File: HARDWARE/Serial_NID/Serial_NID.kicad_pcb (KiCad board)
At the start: 2 copper layers, 40 x 20.3 mm, 14 parts, among them J1 CONN_01X04, J2 CONN_01X07, J3 USB_OTG, U1 TPS2550, U2 STM32L011Gx, U3 FT230XQ

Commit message: updated pcb
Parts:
- added C6: C, ZF_footprints:ZF_SMD_NonPol_0402_cap, F.Cu at (125.2, 104.1)
- added C7: C, ZF_footprints:ZF_SMD_NonPol_0402_cap, F.Cu at (125.2, 103.4)
- added C8: C, ZF_footprints:ZF_SMD_NonPol_0402_cap, F.Cu at (148.6, 105.2)
- added D1: LED, ZF_footprints:ZF_SMD_NonPol_0402, F.Cu at (128.1, 94.4)
- added R4: R, ZF_footprints:ZF_SMD_NonPol_0402, F.Cu at (125.2, 104.9)
- added R5: R, ZF_footprints:ZF_SMD_NonPol_0402, F.Cu at (125.2, 102.6)
- added R6: R, ZF_footprints:ZF_SMD_NonPol_0402, F.Cu at (136.3, 106.8)
- added R7: R, ZF_footprints:ZF_SMD_NonPol_0402, F.Cu at (130.4, 94.4)
- added SW1: SW_PUSH, ZF_footprints:ZF_SW_Momentary_SideMtg, F.Cu at (141.6, 110.5)
- C1, C2, C3, C4, C5: footprint Capacitors_SMD:C_0603_HandSoldering -> ZF_footprints:ZF_SMD_NonPol_0402_cap
- J3: footprint Connectors:USB_Micro-B -> ZF_footprints:JW_USBMICROB_SMT
- R1, R2, R3: footprint Resistors_SMD:R_0603 -> ZF_footprints:ZF_SMD_NonPol_0402
- U2: footprint Housings_DFN_QFN:UQFN-28-1EP_4x4mm_Pitch0.4mm -> ZF_footprints:ZF_IC_UFQFPN28-050
- moved C5 43.3 mm to (148.6, 108.2), turned to 0 degrees
- moved C4 43.2 mm to (148.6, 109.2), turned to 0 degrees
- moved J1 37.1 mm to (160.7, 103.6)
- moved R3 36.4 mm to (153.8, 105.2), turned to 0 degrees
- moved C2 36.1 mm to (144.1, 98.2), turned to 0 degrees
- moved U1 34.9 mm to (149.9, 101.3), turned to 270 degrees
- moved U3 31.0 mm to (129.7, 103.8)
- moved J2 30.9 mm to (141.0, 93.0)
- moved C1 30.9 mm to (129.7, 108.8), turned to 0 degrees
- moved J3 30.0 mm to (119.4, 104.1)
- moved U2 27.9 mm to (139.2, 101.5), turned to 180 degrees
- moved R1 27.3 mm to (134.2, 97.2)
- moved C3 26.3 mm to (125.2, 108.5)
- moved R2 18.7 mm to (129.7, 107.9), turned to 180 degrees
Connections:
- J3 pad 2: Net-(J3-Pad2) -> Net-(C7-Pad1)
- J3 pad 3: Net-(J3-Pad3) -> Net-(C6-Pad2)
- U1 pad 3: +5V -> EN
- U2 pad 10: Net-(U2-Pad10) -> CBUS2
- U2 pad 11: Net-(U2-Pad11) -> CBUS3
- U2 pad 13: Net-(U2-Pad13) -> FAULT
- U2 pad 14: Net-(U2-Pad14) -> EN
- U2 pad 6: Net-(U2-Pad6) -> LED1
- U2 pad 8: Net-(U2-Pad8) -> CBUS0
- U2 pad 9: Net-(U2-Pad9) -> CBUS1
- U3 pad 1: Net-(U3-Pad1) -> +3V3
- U3 pad 11: Net-(U3-Pad11) -> CBUS1
- U3 pad 12: Net-(U3-Pad12) -> CBUS0
- U3 pad 14: Net-(U3-Pad14) -> CBUS3
- U3 pad 5: Net-(U3-Pad5) -> CBUS2
- U3 pad 6: Net-(J3-Pad3) -> Net-(R5-Pad1)
- U3 pad 7: Net-(J3-Pad2) -> Net-(R4-Pad1)
- U3 pad 9: Net-(U3-Pad9) -> +3V3
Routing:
- net EN: track 0.00 -> 23.2 mm
- net FAULT: track 4.23 -> 27.4 mm, vias 0 -> 4
- net +5V: track 33.3 -> 52.0 mm, vias 4 -> 6
- net GND: track 43.7 -> 27.8 mm, vias 2 -> 11
- net A1IN: track 11.3 -> 26.6 mm, vias 0 -> 2
- net SWDIO: track 9.57 -> 22.6 mm, vias 0 -> 2
- net CBUS2: track 0.00 -> 12.9 mm, vias 0 -> 2
- net CBUS1: track 0.00 -> 11.3 mm
- net +3V3: track 25.7 -> 35.9 mm, vias 0 -> 5
- net LED1: track 0.00 -> 9.76 mm
- net CBUS0: track 0.00 -> 9.61 mm
- net SWITCH: track 0.00 -> 8.66 mm, vias 0 -> 2
- net SWCLK: track 9.74 -> 17.6 mm, vias 0 -> 2
- net +5VD: track 29.2 -> 36.6 mm, vias 3 -> 4
- net A1EX: track 13.4 -> 20.7 mm
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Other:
- board size 40 x 20.3 mm -> 48.7 x 24 mm
- net class Default: trace_width 0.15 -> 0.2
- net class POWEr added: clearance 0.1, trace_width 0.5, via_dia 0.6, via_drill 0.4
- rule pad_to_mask_clearance: 0.2 -> 0
- rule trace_min: 0.1 -> 0.2
- board text added: "ID"
- board text added: "Supplying Power 450 mA limited"
- board text added: "USB Power + Network Interface"

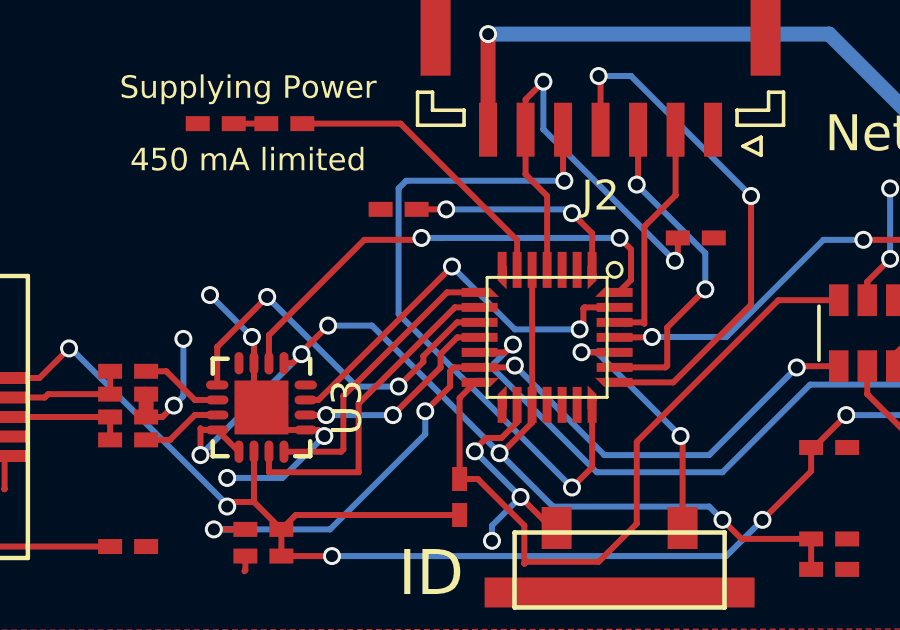
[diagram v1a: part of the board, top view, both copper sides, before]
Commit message: updated TX RX
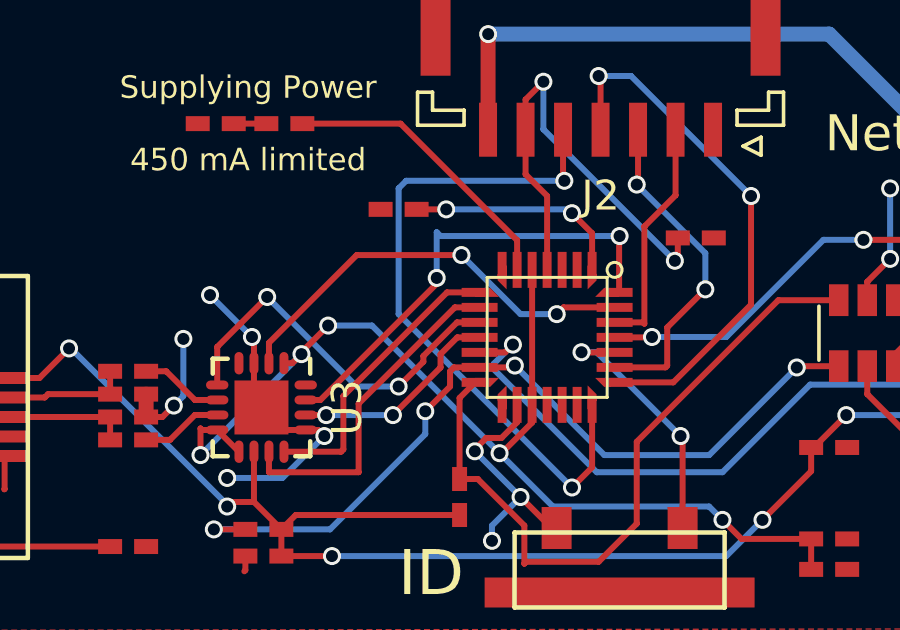
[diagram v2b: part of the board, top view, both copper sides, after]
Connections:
- U2 pad 27: USART2_RX -> USART2_TX
- U2 pad 28: USART2_TX -> USART2_RX
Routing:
- net USART2_RX: track 13.6 -> 15.8 mm
- net USART2_TX: track 16.1 -> 14.3 mm
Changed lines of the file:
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@@
     (links 75)
     (no_connects 3)
-    (area 0 0 0 0)
+    (area 115.773999 87.452999 164.550001 111.550001)
     (thickness 1.6)
     (drawings 9)
-    (tracks 307)
+    (tracks 306)
     (zones 0)
     (modules 23)
@@
       (net 12 MOSI))
     (pad 27 smd rect (at -2.246733 0.986815 90) (size 0.3 1.2) (layers F.Cu F.Paste F.Mask)
+      (net 37 USART2_TX))
+    (pad 28 smd rect (at -2.396733 1.486815 90) (size 0.3 0.9) (layers F.Cu F.Paste F.Mask)
       (net 36 USART2_RX))
-    (pad 28 smd rect (at -2.396733 1.486815 90) (size 0.3 0.9) (layers F.Cu F.Paste F.Mask)
-      (net 37 USART2_TX))
     (pad 1 smd trapezoid (at -1.496733 1.986815) (size 0.3 0.5) (rect_delta 0.3 0 ) (layers F.Cu F.Paste F.Mask)
       (net 17 "Net-(R1-Pad1)"))
     (pad 28 smd trapezoid (at -1.996733 1.486815 90) (size 0.3 0.5) (rect_delta 0.3 0 ) (layers F.Cu F.Paste F.Mask)
-      (net 37 USART2_TX))
+      (net 36 USART2_RX))
     (pad 14 smd trapezoid (at 2.003267 -1.513185 270) (size 0.3 0.5) (rect_delta 0.3 0 ) (layers F.Cu F.Paste F.Mask)
       (net 22 EN))
@@
   (via (at 131.826 104.0765) (size 0.6) (drill 0.4) (layers F.Cu B.Cu) (net 31))
   (segment (start 131.822 104.0725) (end 131.826 104.0765) (width 0.2) (layer F.Cu) (net 31))
-  (segment (start 131.142 103.5725) (end 131.568 103.5725) (width 0.2) (layer F.Cu) (net 36))
-  (segment (start 140.432815 100.486185) (end 141.438733 100.486185) (width 0.2) (layer F.Cu) (net 36))
-  (segment (start 140.3985 100.5205) (end 140.432815 100.486185) (width 0.2) (layer F.Cu) (net 36))
-  (segment (start 140.3985 101.092) (end 140.3985 100.5205) (width 0.2) (layer F.Cu) (net 36))
-  (segment (start 140.2715 101.219) (end 140.3985 101.092) (width 0.2) (layer F.Cu) (net 36))
-  (via (at 140.2715 101.219) (size 0.6) (drill 0.4) (layers F.Cu B.Cu) (net 36))
-  (segment (start 138.1125 101.219) (end 140.2715 101.219) (width 0.2) (layer B.Cu) (net 36))
-  (segment (start 136.017 99.1235) (end 138.1125 101.219) (width 0.2) (layer B.Cu) (net 36))
-  (via (at 136.017 99.1235) (size 0.6) (drill 0.4) (layers F.Cu B.Cu) (net 36))
-  (segment (start 131.568 103.5725) (end 136.017 99.1235) (width 0.2) (layer F.Cu) (net 36))
-  (segment (start 141.588733 99.986185) (end 141.588733 99.965267) (width 0.2) (layer F.Cu) (net 37))
-  (segment (start 141.588733 99.965267) (end 141.986 99.568) (width 0.2) (layer F.Cu) (net 37))
-  (segment (start 141.986 99.568) (end 141.986 98.552) (width 0.2) (layer F.Cu) (net 37))
-  (segment (start 141.986 98.552) (end 141.605 98.171) (width 0.2) (layer F.Cu) (net 37))
-  (via (at 141.605 98.171) (size 0.6) (drill 0.4) (layers F.Cu B.Cu) (net 37))
-  (segment (start 141.605 98.171) (end 135.636 98.171) (width 0.2) (layer B.Cu) (net 37))
-  (segment (start 135.636 98.171) (end 135.001 98.171) (width 0.2) (layer B.Cu) (net 37))
-  (via (at 135.001 98.171) (size 0.6) (drill 0.4) (layers F.Cu B.Cu) (net 37))
-  (segment (start 135.001 98.171) (end 134.9375 98.2345) (width 0.2) (layer F.Cu) (net 37))
-  (segment (start 134.9375 98.2345) (end 133.096 98.2345) (width 0.2) (layer F.Cu) (net 37))
-  (segment (start 133.096 98.2345) (end 129.917 101.4135) (width 0.2) (layer F.Cu) (net 37))
-  (segment (start 129.917 101.4135) (end 129.917 102.3475) (width 0.2) (layer F.Cu) (net 37))
+  (segment (start 131.142 103.5725) (end 131.6315 103.5725) (width 0.2) (layer F.Cu) (net 36) (status 400000))
+  (segment (start 141.588733 98.123767) (end 141.588733 99.986185) (width 0.2) (layer F.Cu) (net 36) (status 800000))
+  (segment (start 141.605 98.1075) (end 141.588733 98.123767) (width 0.2) (layer F.Cu) (net 36))
+  (via (at 141.605 98.1075) (size 0.6) (drill 0.4) (layers F.Cu B.Cu) (net 36))
+  (segment (start 135.636 98.1075) (end 141.605 98.1075) (width 0.2) (layer B.Cu) (net 36))
+  (segment (start 135.509 97.9805) (end 135.636 98.1075) (width 0.2) (layer B.Cu) (net 36))
+  (segment (start 135.509 99.5045) (end 135.509 97.9805) (width 0.2) (layer B.Cu) (net 36))
+  (via (at 135.509 99.5045) (size 0.6) (drill 0.4) (layers F.Cu B.Cu) (net 36))
+  (segment (start 135.5725 99.568) (end 135.509 99.5045) (width 0.2) (layer F.Cu) (net 36))
+  (segment (start 135.5725 99.6315) (end 135.5725 99.568) (width 0.2) (layer F.Cu) (net 36))
+  (segment (start 131.6315 103.5725) (end 135.5725 99.6315) (width 0.2) (layer F.Cu) (net 36))
+  (segment (start 141.588733 99.986185) (end 141.588733 99.965267) (width 0.2) (layer F.Cu) (net 36))
+  (segment (start 129.917 102.3475) (end 129.917 101.6675) (width 0.2) (layer F.Cu) (net 37) (status 400000))
+  (segment (start 139.734315 100.486185) (end 141.438733 100.486185) (width 0.2) (layer F.Cu) (net 37) (status 800000))
+  (segment (start 139.5095 100.711) (end 139.734315 100.486185) (width 0.2) (layer F.Cu) (net 37))
+  (via (at 139.5095 100.711) (size 0.6) (drill 0.4) (layers F.Cu B.Cu) (net 37))
+  (segment (start 138.303 100.711) (end 139.5095 100.711) (width 0.2) (layer B.Cu) (net 37))
+  (segment (start 136.3345 98.7425) (end 138.303 100.711) (width 0.2) (layer B.Cu) (net 37))
+  (via (at 136.3345 98.7425) (size 0.6) (drill 0.4) (layers F.Cu B.Cu) (net 37))
+  (segment (start 132.842 98.7425) (end 136.3345 98.7425) (width 0.2) (layer F.Cu) (net 37))
+  (segment (start 129.917 101.6675) (end 132.842 98.7425) (width 0.2) (layer F.Cu) (net 37))
   (zone (net 1) (net_name GND) (layer F.Cu) (hatch edge 0.508)
     (connect_pads (clearance 0.508))

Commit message: fixed pcb
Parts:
- added C10: C, ZF_footprints:ZF_SMD_NonPol_0402_cap, F.Cu at (129.7, 109.7)
- added C9: C, ZF_footprints:ZF_SMD_NonPol_0402_cap, F.Cu at (129.7, 110.7)
- J1: footprint Connectors_JST:JST_GH_SM04B-GHS-TB_04x1.25mm_Angled -> ZF_footprints:ZF_CONN_JST_GH
- J2: footprint Connectors_JST:JST_GH_SM07B-GHS-TB_07x1.25mm_Angled -> ZF_footprints:ZF_CONN_JST_GH_7POS
- U3: footprint Housings_DFN_QFN:QFN-16-1EP_3x3mm_Pitch0.5mm -> Housings_DFN_QFN:QFN-16-1EP_4x4mm_Pitch0.65mm
- moved J2 2.39 mm to (141.4, 90.6), turned to 90 degrees
- moved J1 1.98 mm to (162.2, 102.4), turned to 0 degrees
- moved U3 0.63 mm to (130.3, 103.8)
- moved SW1 0.51 mm to (141.6, 111.0)
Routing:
- net CBUS0: track 9.61 -> 25.3 mm, vias 0 -> 2
- net CBUS1: track 11.3 -> 22.6 mm, vias 0 -> 2
- net GND: track 27.8 -> 38.8 mm, vias 11 -> 10
- net +3V3: track 35.9 -> 46.7 mm, vias 5 -> 6
- net +5V: track 52.0 -> 54.0 mm
- net NSS: track 11.1 -> 12.9 mm
- net MOSI: track 7.90 -> 9.69 mm
- net SWDIO: track 22.6 -> 24.3 mm
- net A1IN: track 26.6 -> 28.0 mm
- net SWCLK: track 17.6 -> 16.4 mm
- net CBUS3: track 7.13 -> 6.19 mm, vias 2 -> 0
- net USART2_TX: track 14.3 -> 13.5 mm
- net SWITCH: track 8.66 -> 9.26 mm
- net EN: track 23.2 -> 23.8 mm
- added copper zone on B.Cu, net GND
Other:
- board size 48.7 x 24 mm -> 47.5 x 23 mm
- net class Default: clearance 0.1 -> 0.2
- net class POWEr: clearance 0.1 -> 0.2
- rule trace_clearance: 0.1 -> 0.2

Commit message: fixed pcb
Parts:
- added G***: LOGO, ZF_footprints:ZF_LOGO_OSHW, F.Cu at (121.5, 95.1)
- C10: value C -> 4.7uF; footprint ZF_footprints:ZF_SMD_NonPol_0402_cap -> Resistors_SMD:R_0603_HandSoldering
- J3: footprint ZF_footprints:JW_USBMICROB_SMT -> ZF_footprints:ZF_CONN_USB-MICRO-B-SMD-holes
- moved C10 4.93 mm to (134.6, 110.4)
- moved C9 1.02 mm to (129.7, 109.7)
- moved J3 0.83 mm to (118.6, 104.1)
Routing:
- net GND: track 38.8 -> 34.4 mm, vias 10 -> 8
- net A1IN: track 28.0 -> 29.9 mm
- net Net-(C3-Pad1): track 13.8 -> 15.4 mm
- net +5V: track 54.0 -> 55.4 mm
- net +3V3: track 46.7 -> 47.8 mm

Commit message: fixd pcb
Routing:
- net +5V: track 55.4 -> 56.2 mm
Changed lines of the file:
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@@
   (general
     (links 83)
-    (no_connects 1)
-    (area 116.949999 88.449999 164.550001 111.550001)
+    (no_connects 0)
+    (area 111.8295 85.581166 167.212334 114.300001)
     (thickness 1.6)
     (drawings 7)
-    (tracks 371)
+    (tracks 366)
     (zones 0)
     (modules 26)
@@
     (46 B.CrtYd user)
     (47 F.CrtYd user)
-    (48 B.Fab user)
-    (49 F.Fab user)
+    (48 B.Fab user hide)
+    (49 F.Fab user hide)
   )
   (setup
@@
     (effects (font (size 1.33 1.33) (thickness 0.19) italic))
   )
-  (segment (start 126.4285 102.9335) (end 126.365 102.9335) (width 0.2) (layer B.Cu) (net 0))
-  (segment (start 126.365 102.997) (end 126.365 102.9335) (width 0.2) (layer B.Cu) (net 0))
   (segment (start 134.239 108.0135) (end 131.8895 110.363) (width 0.2) (layer F.Cu) (net 1))
   (via (at 136.906 105.41) (size 0.6) (drill 0.4) (layers F.Cu B.Cu) (net 1))
   (via (at 131.8895 110.363) (size 0.6) (drill 0.4) (layers F.Cu B.Cu) (net 1))
-  (segment (start 131.8895 110.363) (end 131.6355 110.617) (width 0.2) (layer B.Cu) (net 1))
   (segment (start 135.0645 106.3625) (end 135.0645 107.188) (width 0.2) (layer B.Cu) (net 1))
   (segment (start 136.144 105.283) (end 135.0645 106.3625) (width 0.2) (layer B.Cu) (net 1))
@@
   (segment (start 149.86 99.6315) (end 150.622 98.8695) (width 0.2) (layer F.Cu) (net 1))
   (segment (start 125.822 104.14) (end 125.822 103.378) (width 0.5) (layer F.Cu) (net 1))
+  (segment (start 130.3305 109.6645) (end 130.3305 108.7755) (width 0.2) (layer F.Cu) (net 2) (status C00000))
   (segment (start 135.72 110.363) (end 135.72 108.4785) (width 0.2) (layer F.Cu) (net 2))
   (segment (start 135.72 108.4785) (end 134.6485 107.407) (width 0.2) (layer F.Cu) (net 2))
@@
   (segment (start 158.272 100.487) (end 159.779 100.487) (width 0.2) (layer F.Cu) (net 11))
   (segment (start 156.0195 98.2345) (end 156.083 98.298) (width 0.2) (layer F.Cu) (net 11))
+  (segment (start 143.47 96.7505) (end 143.8275 96.393) (width 0.2) (layer F.Cu) (net 12))
+  (segment (start 142.218815 100.986185) (end 142.4305 100.7745) (width 0.2) (layer F.Cu) (net 12))
+  (segment (start 142.4305 100.7745) (end 142.4305 97.79) (width 0.2) (layer F.Cu) (net 12))
+  (segment (start 143.47 96.7505) (end 142.4305 97.79) (width 0.2) (layer F.Cu) (net 12))
   (segment (start 141.438733 100.986185) (end 142.218815 100.986185) (width 0.2) (layer F.Cu) (net 12))
-  (segment (start 143.47 96.7505) (end 142.4305 97.79) (width 0.2) (layer F.Cu) (net 12))
-  (segment (start 143.47 96.7505) (end 143.47 94.615) (width 0.2) (layer F.Cu) (net 12))
-  (segment (start 142.4305 100.7745) (end 142.4305 97.79) (width 0.2) (layer F.Cu) (net 12))
-  (segment (start 142.218815 100.986185) (end 142.4305 100.7745) (width 0.2) (layer F.Cu) (net 12))
-  (segment (start 143.47 94.615) (end 143.47 93.459) (width 0.2) (layer F.Cu) (net 12))
-  (segment (start 143.47 93.459) (end 143.9145 93.0145) (width 0.2) (layer F.Cu) (net 12))
-  (segment (start 143.47 94.564) (end 143.47 94.615) (width 0.2) (layer F.Cu) (net 12))
-  (segment (start 142.22 94.615) (end 142.22 93.459) (width 0.2) (layer F.Cu) (net 13))
-  (segment (start 142.22 93.459) (end 142.6645 93.0145) (width 0.2) (layer F.Cu) (net 13))
-  (segment (start 142.22 94.564) (end 142.22 94.615) (width 0.2) (layer F.Cu) (net 13))
-  (segment (start 142.22 94.615) (end 142.22 96.3495) (width 0.2) (layer F.Cu) (net 13))
-  (segment (start 143.131815 102.486185) (end 141.438733 102.486185) (width 0.2) (layer F.Cu) (net 13))
+  (segment (start 143.8275 96.393) (end 143.8275 93.1015) (width 0.2) (layer F.Cu) (net 12) (status 800000))
+  (segment (start 143.8275 93.1015) (end 143.9145 93.0145) (width 0.2) (layer F.Cu) (net 12) (status C00000))
+  (segment (start 144.4625 98.679) (end 144.4625 98.2345) (width 0.2) (layer B.Cu) (net 13))
+  (segment (start 144.4625 98.679) (end 144.4625 99.8855) (width 0.2) (layer B.Cu) (net 13))
+  (via (at 144.4625 99.8855) (size 0.6) (drill 0.4) (layers F.Cu B.Cu) (net 13))
+  (segment (start 144.4625 99.8855) (end 143.7005 100.6475) (width 0.2) (layer F.Cu) (net 13))
+  (segment (start 143.7005 100.6475) (end 143.7005 101.9175) (width 0.2) (layer F.Cu) (net 13))
   (segment (start 143.7005 101.9175) (end 143.131815 102.486185) (width 0.2) (layer F.Cu) (net 13))
-  (segment (start 143.7005 100.6475) (end 143.7005 101.9175) (width 0.2) (layer F.Cu) (net 13))
-  (segment (start 144.4625 99.8855) (end 143.7005 100.6475) (width 0.2) (layer F.Cu) (net 13))
-  (via (at 144.4625 99.8855) (size 0.6) (drill 0.4) (layers F.Cu B.Cu) (net 13))
-  (segment (start 144.4625 98.679) (end 144.4625 99.8855) (width 0.2) (layer B.Cu) (net 13))
-  (segment (start 142.1765 96.393) (end 144.4625 98.679) (width 0.2) (layer B.Cu) (net 13))
-  (via (at 142.1765 96.393) (size 0.6) (drill 0.4) (layers F.Cu B.Cu) (net 13))
-  (segment (start 142.22 96.3495) (end 142.1765 96.393) (width 0.2) (layer F.Cu) (net 13))
+  (segment (start 141.438733 102.486185) (end 143.131815 102.486185) (width 0.2) (layer F.Cu) (net 13))
+  (segment (start 142.6645 96.3495) (end 142.6645 93.0145) (width 0.2) (layer F.Cu) (net 13) (status 800000))
+  (segment (start 142.621 96.393) (end 142.6645 96.3495) (width 0.2) (layer F.Cu) (net 13))
+  (via (at 142.621 96.393) (size 0.6) (drill 0.4) (layers F.Cu B.Cu) (net 13))
+  (segment (start 144.4625 98.2345) (end 142.621 96.393) (width 0.2) (layer B.Cu) (net 13))
   (segment (start 145.9865 96.774) (end 145.923 96.774) (width 0.2) (layer B.Cu) (net 14))
   (segment (start 143.393815 102.986185) (end 145.9865 100.3935) (width 0.2) (layer F.Cu) (net 14))
@@
   (segment (start 144.145 94.996) (end 141.4145 94.996) (width 0.2) (layer B.Cu) (net 14))
   (segment (start 145.923 96.774) (end 144.145 94.996) (width 0.2) (layer B.Cu) (net 14))
-  (segment (start 139.72 94.564) (end 139.72 93.459) (width 0.2) (layer F.Cu) (net 15))
+  (segment (start 139.7635 96.266) (end 140.1445 95.885) (width 0.2) (layer F.Cu) (net 15))
+  (segment (start 140.1445 95.885) (end 140.1445 93.0345) (width 0.2) (layer F.Cu) (net 15) (status 800000))
+  (segment (start 140.1445 93.0345) (end 140.1645 93.0145) (width 0.2) (layer F.Cu) (net 15) (status C00000))
   (segment (start 140.688733 105.818267) (end 140.0175 106.4895) (width 0.2) (layer F.Cu) (net 15))
   (via (at 140.0175 106.4895) (size 0.6) (drill 0.4) (layers F.Cu B.Cu) (net 15))
@@
   (via (at 139.7635 96.266) (size 0.6) (drill 0.4) (layers F.Cu B.Cu) (net 15))
   (segment (start 139.7635 96.266) (end 139.72 96.2225) (width 0.2) (layer F.Cu) (net 15))
-  (segment (start 139.72 96.2225) (end 139.72 94.564) (width 0.2) (layer F.Cu) (net 15))
   (segment (start 140.688733 103.886185) (end 140.688733 105.818267) (width 0.2) (layer F.Cu) (net 15))
-  (segment (start 139.72 93.459) (end 140.1645 93.0145) (width 0.2) (layer F.Cu) (net 15))
   (segment (start 140.688733 99.086185) (end 140.688733 98.016733) (width 0.2) (layer F.Cu) (net 17))
   (segment (start 135.8265 97.2185) (end 134.839 97.2185) (width 0.2) (layer F.Cu) (net 17))
